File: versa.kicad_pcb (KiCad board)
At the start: 2 copper layers, 52.2 x 54.4 mm, 69 parts, among them SW1 Flash Button, SW2 Button, SW4 Reset Button, U1 NCP1117-3.3_SOT223, Y1 12 MHz

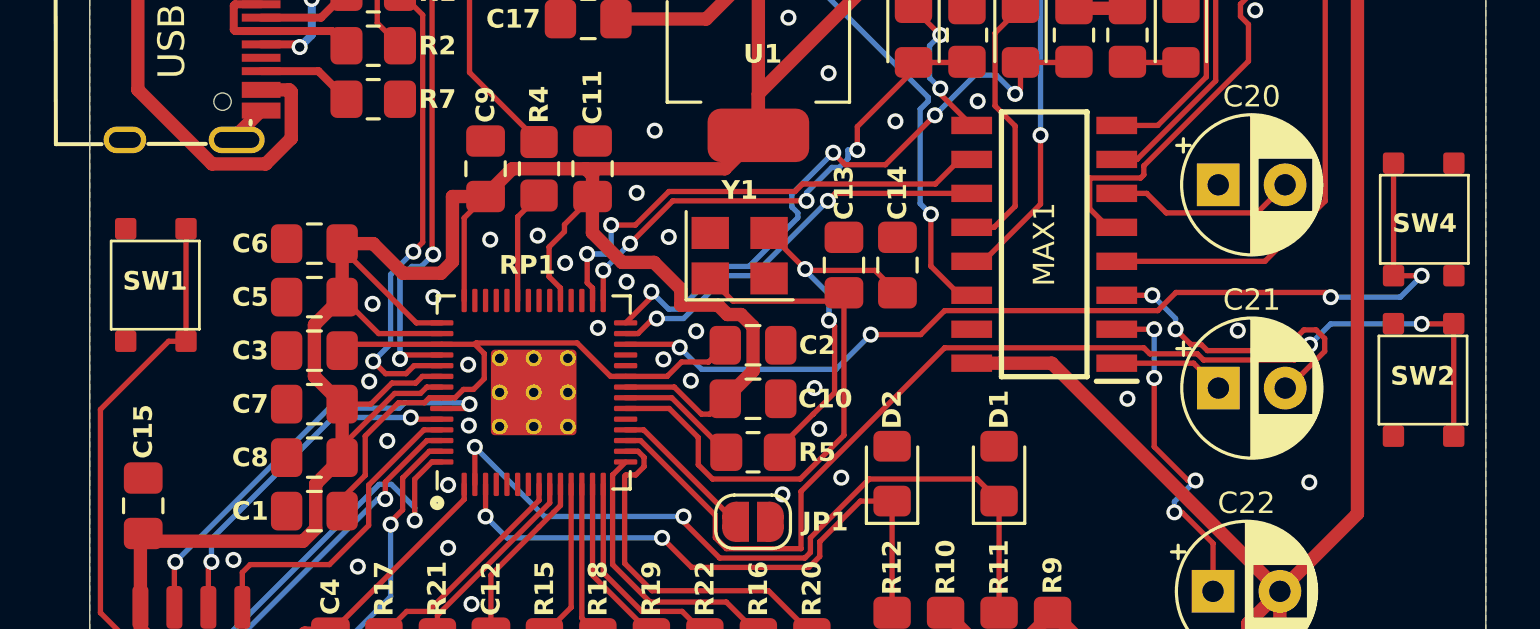
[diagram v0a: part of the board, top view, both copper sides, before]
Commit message: Updated silkscreen
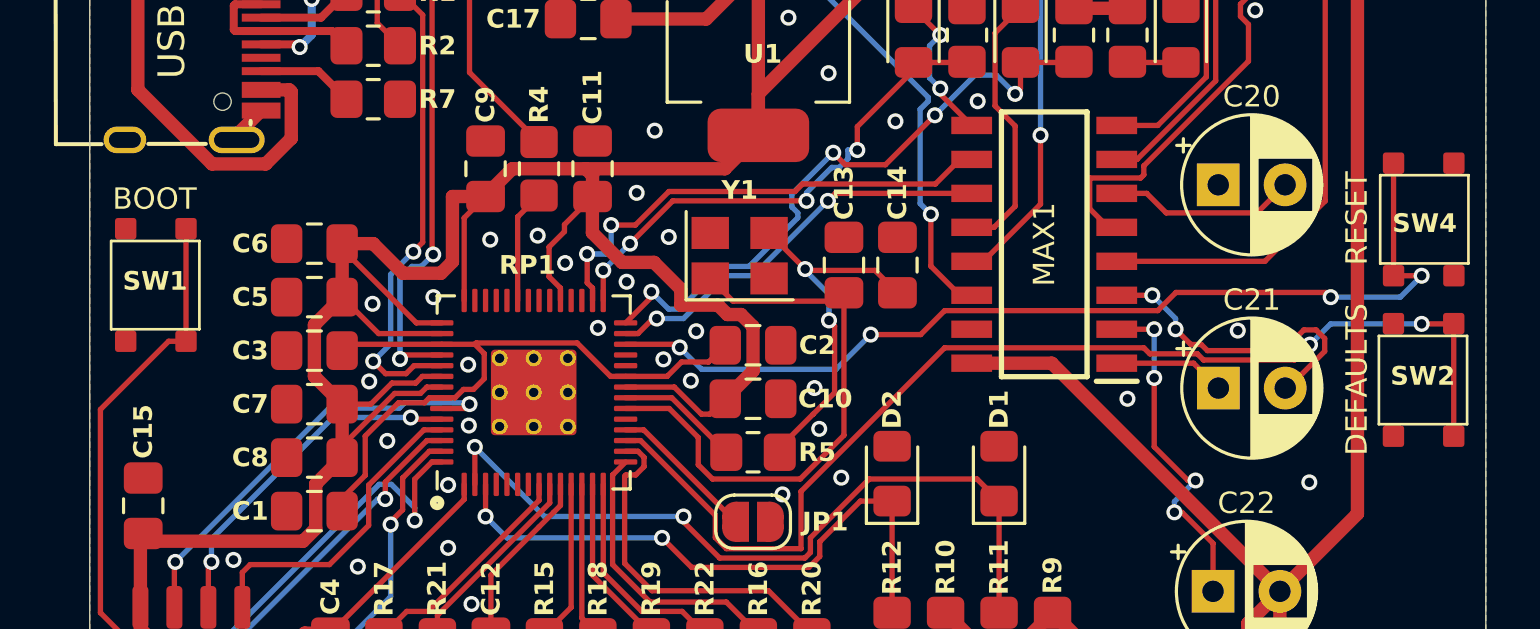
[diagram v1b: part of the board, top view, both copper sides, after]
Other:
- board text added: "BOOT"
- board text added: "DEFAULTS"
- board text added: "RESET"
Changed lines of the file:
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@@
+		)
+	)
+	(gr_text "BOOT"
+		(at 168.025 74.125 0)
+		(layer "F.SilkS")
+		(effects
+			(font
+				(size 0.8 0.8)
+				(thickness 0.13)
+			)
+		)
+	)
+	(gr_text "RESET"
+		(at 212.975 74.85 90)
+		(layer "F.SilkS")
+		(effects
+			(font
+				(size 0.8 0.8)
+				(thickness 0.13)
+			)
+		)
+	)
+	(gr_text "DEFAULTS"
+		(at 212.975 80.875 90)
+		(layer "F.SilkS")
+		(effects
+			(font
+				(size 0.8 0.8)
+				(thickness 0.13)
+			)
 		)
 	)
